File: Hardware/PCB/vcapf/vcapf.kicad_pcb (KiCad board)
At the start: 2 copper layers, 10 parts, among them J1 Synth_power_2x5

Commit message: Post breadboard tweaks; layout
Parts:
- removed the C2 at (238.3, 117.1)
- added C10: 100nF, ao_tht:C_Disc_D3.0mm_W1.6mm_P2.50mm, B.Cu at (111.4, 138.1)
- added C11: 100nF, ao_tht:C_Rect_L7.2mm_W2.5mm_P5.00mm_FKS2_FKP2_MKS2_MKP2, B.Cu at (84.8, 91.1)
- added C3: 100nF, ao_tht:C_Rect_L7.2mm_W2.5mm_P5.00mm_FKS2_FKP2_MKS2_MKP2, B.Cu at (115.2, 91.1)
- added C5: 100nF, ao_tht:C_Disc_D3.0mm_W1.6mm_P2.50mm, B.Cu at (111.5, 59.0)
- added C6: 4.7nF, ao_tht:C_Disc_D5.0mm_W2.5mm_P5.00mm, B.Cu at (86.0, 136.8)
- added C7: 100nF, ao_tht:C_Disc_D3.0mm_W1.6mm_P2.50mm, B.Cu at (91.1, 91.1)
- added C8: 100nF, ao_tht:C_Disc_D3.0mm_W1.6mm_P2.50mm, B.Cu at (111.4, 91.1)
- added C9: 100nF, ao_tht:C_Disc_D3.0mm_W1.6mm_P2.50mm, B.Cu at (96.2, 122.9)
- added D3: 1N4148, ao_tht:D_DO-35_SOD27_P7.62mm_Horizontal, B.Cu at (88.6, 74.6)
- added GRAF1: Holes, vcapf:vcapf_panel_holes, F.Cu at (100.0, 100.0)
- added GRAF2: CC0 logo, ao_tht:CC0_logo, F.Cu at (119.0, 169.1)
- added GRAF3: AO logo, ao_tht:analogoutput, B.Cu at (99.5, 75.0)
- added H1: MountingHole, ao_tht:MountingHole_3.2mm_M3, F.Cu at (80.0, 139.0)
- added H2: MountingHole, ao_tht:MountingHole_3.2mm_M3, F.Cu at (120.0, 139.0)
- added H3: MountingHole, ao_tht:MountingHole_3.2mm_M3, F.Cu at (180.0, 139.0)
- added H4: MountingHole, ao_tht:MountingHole_3.2mm_M3, F.Cu at (220.0, 139.0)
- added J2: AudioJack2, ao_tht:Jack_6.35mm_PJ_629HAN_slots, F.Cu at (187.5, 150.0)
- added J3: AudioJack2, ao_tht:Jack_6.35mm_PJ_629HAN_slots, F.Cu at (212.5, 150.0)
- added J4: Conn_01x05, Connector_PinSocket_2.54mm:PinSocket_1x05_P2.54mm_Vertical, B.Cu at (95.0, 138.5)
- added J5: Conn_01x05, Connector_PinHeader_2.54mm:PinHeader_1x05_P2.54mm_Vertical, F.Cu at (195.0, 138.5)
- added J6: AudioJack2, ao_tht:Jack_6.35mm_PJ_629HAN_slots, F.Cu at (187.5, 175.0)
- added J7: AudioJack2, ao_tht:Jack_6.35mm_PJ_629HAN_slots, F.Cu at (212.5, 175.0)
- added Q1: 2N3906, ao_tht:TO-92_Inline_Wide, B.Cu at (81.0, 120.0)
- added Q2: 2N3906, ao_tht:TO-92_Inline_Wide, B.Cu at (81.0, 112.3)
- added R1: 100k, ao_tht:R_Axial_DIN0207_L6.3mm_D2.5mm_P10.16mm_Horizontal, B.Cu at (119.0, 55.5)
- added R10: 4.7k, ao_tht:R_Axial_DIN0207_L6.3mm_D2.5mm_P10.16mm_Horizontal, B.Cu at (81.0, 126.7)
- added R11: 100k, ao_tht:R_Axial_DIN0207_L6.3mm_D2.5mm_P10.16mm_Horizontal, B.Cu at (81.0, 55.5)
- added R12: 620R, ao_tht:R_Axial_DIN0207_L6.3mm_D2.5mm_P10.16mm_Horizontal, B.Cu at (91.1, 51.7)
- added R13: 100k, ao_tht:R_Axial_DIN0207_L6.3mm_D2.5mm_P10.16mm_Horizontal, B.Cu at (81.0, 87.3)
- added R14: 620R, ao_tht:R_Axial_DIN0207_L6.3mm_D2.5mm_P10.16mm_Horizontal, B.Cu at (91.1, 47.9)
- added R15: 6.8k, ao_tht:R_Axial_DIN0207_L6.3mm_D2.5mm_P10.16mm_Horizontal, B.Cu at (81.0, 44.1)
- added R16: 30k, ao_tht:R_Axial_DIN0207_L6.3mm_D2.5mm_P10.16mm_Horizontal, B.Cu at (108.9, 98.7)
- added R17: 15k, ao_tht:R_Axial_DIN0207_L6.3mm_D2.5mm_P10.16mm_Horizontal, B.Cu at (108.9, 94.9)
- added R18: 30k, ao_tht:R_Axial_DIN0207_L6.3mm_D2.5mm_P10.16mm_Horizontal, B.Cu at (91.1, 102.5)
- added R19: 7.5k, ao_tht:R_Axial_DIN0207_L6.3mm_D2.5mm_P10.16mm_Horizontal, B.Cu at (91.1, 98.7)
- added R2: 470k, ao_tht:R_Axial_DIN0207_L6.3mm_D2.5mm_P10.16mm_Horizontal, B.Cu at (81.0, 70.8)
- added R20: 7.5k, ao_tht:R_Axial_DIN0207_L6.3mm_D2.5mm_P10.16mm_Horizontal, B.Cu at (91.1, 94.9)
- added R21: 10k, ao_tht:R_Axial_DIN0207_L6.3mm_D2.5mm_P10.16mm_Horizontal, B.Cu at (108.9, 126.7)
- added R22: 30k, ao_tht:R_Axial_DIN0207_L6.3mm_D2.5mm_P10.16mm_Horizontal, B.Cu at (119.0, 102.5)
- added R23: 30k, ao_tht:R_Axial_DIN0207_L6.3mm_D2.5mm_P10.16mm_Horizontal, B.Cu at (81.0, 106.3)
- added R24: 10k, ao_tht:R_Axial_DIN0207_L6.3mm_D2.5mm_P10.16mm_Horizontal, B.Cu at (119.0, 131.8)
- added R25: 100k, ao_tht:R_Axial_DIN0207_L6.3mm_D2.5mm_P10.16mm_Horizontal, B.Cu at (195.2, 163.5)
- added R26: 100k, ao_tht:R_Axial_DIN0207_L6.3mm_D2.5mm_P10.16mm_Horizontal, B.Cu at (209.2, 163.5)
- added R27: 1k, ao_tht:R_Axial_DIN0207_L6.3mm_D2.5mm_P10.16mm_Horizontal, B.Cu at (190.2, 163.5)
- added R28: 1k, ao_tht:R_Axial_DIN0207_L6.3mm_D2.5mm_P10.16mm_Horizontal, B.Cu at (200.3, 167.3)
- added R3: 100k, ao_tht:R_Axial_DIN0207_L6.3mm_D2.5mm_P10.16mm_Horizontal, B.Cu at (91.1, 78.4)
- added R4: 2.7k, ao_tht:R_Axial_DIN0207_L6.3mm_D2.5mm_P10.16mm_Horizontal, B.Cu at (81.0, 82.2)
- added R5: 620R, ao_tht:R_Axial_DIN0207_L6.3mm_D2.5mm_P10.16mm_Horizontal, B.Cu at (108.9, 51.7)
- added R6: 100k, ao_tht:R_Axial_DIN0207_L6.3mm_D2.5mm_P10.16mm_Horizontal, B.Cu at (119.0, 87.3)
- added R7: 620R, ao_tht:R_Axial_DIN0207_L6.3mm_D2.5mm_P10.16mm_Horizontal, B.Cu at (108.9, 47.9)
- added R8: 470k, ao_tht:R_Axial_DIN0207_L6.3mm_D2.5mm_P10.16mm_Horizontal, B.Cu at (81.0, 131.8)
- added R9: 6.8k, ao_tht:R_Axial_DIN0207_L6.3mm_D2.5mm_P10.16mm_Horizontal, B.Cu at (119.0, 44.1)
- added RV1: 100k, ao_tht:Potentiometer_Alpha_16mm_Single_Vertical, F.Cu at (100.0, 115.0)
- added RV2: 100k, ao_tht:Potentiometer_Alpha_16mm_Single_Vertical, F.Cu at (100.0, 30.0)
- added RV3: 100k, ao_tht:Potentiometer_Alpha_16mm_Single_Vertical, F.Cu at (99.7, 75.0)
- added U1: LM13700, ao_tht:DIP-16_W7.62mm_Socket_LongPads, B.Cu at (103.8, 44.1)
- added U2: TL074, ao_tht:DIP-14_W7.62mm_Socket_LongPads, B.Cu at (96.2, 102.5)
- added U3: TL072, ao_tht:DIP-8_W7.62mm_Socket_LongPads, B.Cu at (103.8, 126.7)
- C1, C4, D1, D2, J1: moved to B.Cu
- C2: renamed from C3; moved to B.Cu
- TP1: value TestPoint -> +12V; moved to B.Cu
- TP2: value TestPoint -> GND; footprint ao_tht:TestPoint_THTPad_D1.5mm_Drill0.7mm -> ao_tht:TestPoint_THTPad_1.5x1.5mm_Drill0.7mm; moved to B.Cu
- TP3: value TestPoint -> -12V; moved to B.Cu
- moved TP3 202.7 mm to (78.4, 25.1), turned to 90 degrees
- moved TP2 202.6 mm to (78.4, 32.7), turned to 90 degrees
- moved TP1 193.0 mm to (78.4, 40.3), turned to 90 degrees
- moved C1 189.1 mm to (82.2, 18.7)
- moved D2 177.0 mm to (91.1, 20.0)
- moved D1 176.8 mm to (91.1, 16.2)
- moved C2 176.2 mm to (106.3, 18.7)
- moved C4 163.5 mm to (91.0, 59.4), turned to 180 degrees
- moved J1 141.5 mm to (115.2, 34.0)
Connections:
- C4 pad 1: GND -> +12V
- C4 pad 2: -12V -> GND
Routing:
- net -12V: track 0.00 -> 190.1 mm
- net +12V: track 0.00 -> 157.5 mm
- net Net-(Q2-Pad3): track 0.00 -> 109.4 mm
- net /Main PCB/INPUT_ATT: track 0.00 -> 88.3 mm
- net /Main PCB/CV_IN: track 0.00 -> 88.0 mm
- net /Main PCB/LP1: track 0.00 -> 80.3 mm
- net Net-(D3-Pad1): track 0.00 -> 58.7 mm
- net Net-(R11-Pad2): track 0.00 -> 54.4 mm
- net Net-(C11-Pad1): track 0.00 -> 53.6 mm
- net Net-(C3-Pad1): track 0.00 -> 53.6 mm
- net /Main PCB/1POLE_OUT: track 0.00 -> 52.7 mm
- net /Main PCB/INPUT: track 0.00 -> 48.3 mm
- net Net-(R1-Pad2): track 0.00 -> 45.5 mm
- net /Main PCB/FREQ: track 0.00 -> 43.2 mm
- net /2POLE_OUT_J: track 0.00 -> 39.3 mm
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- added copper zone on B.Cu, net GND
- added copper zone on F.Cu, net GND
- added copper zone on B.Cu, net GND1
- added copper zone on F.Cu, net GND1
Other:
- board outline added: 146 x 171 mm
- board text added: "Jacks board"
- board text added: "Rich Holmes / April 2022 CC0 1.0 Main board"
- board text added: "VCAPF"
- board text added: "VOLTAGE CONTROLLED ALL PASS FILTER"
- board text added: "https://github.com/holmesrichards/vcapf"

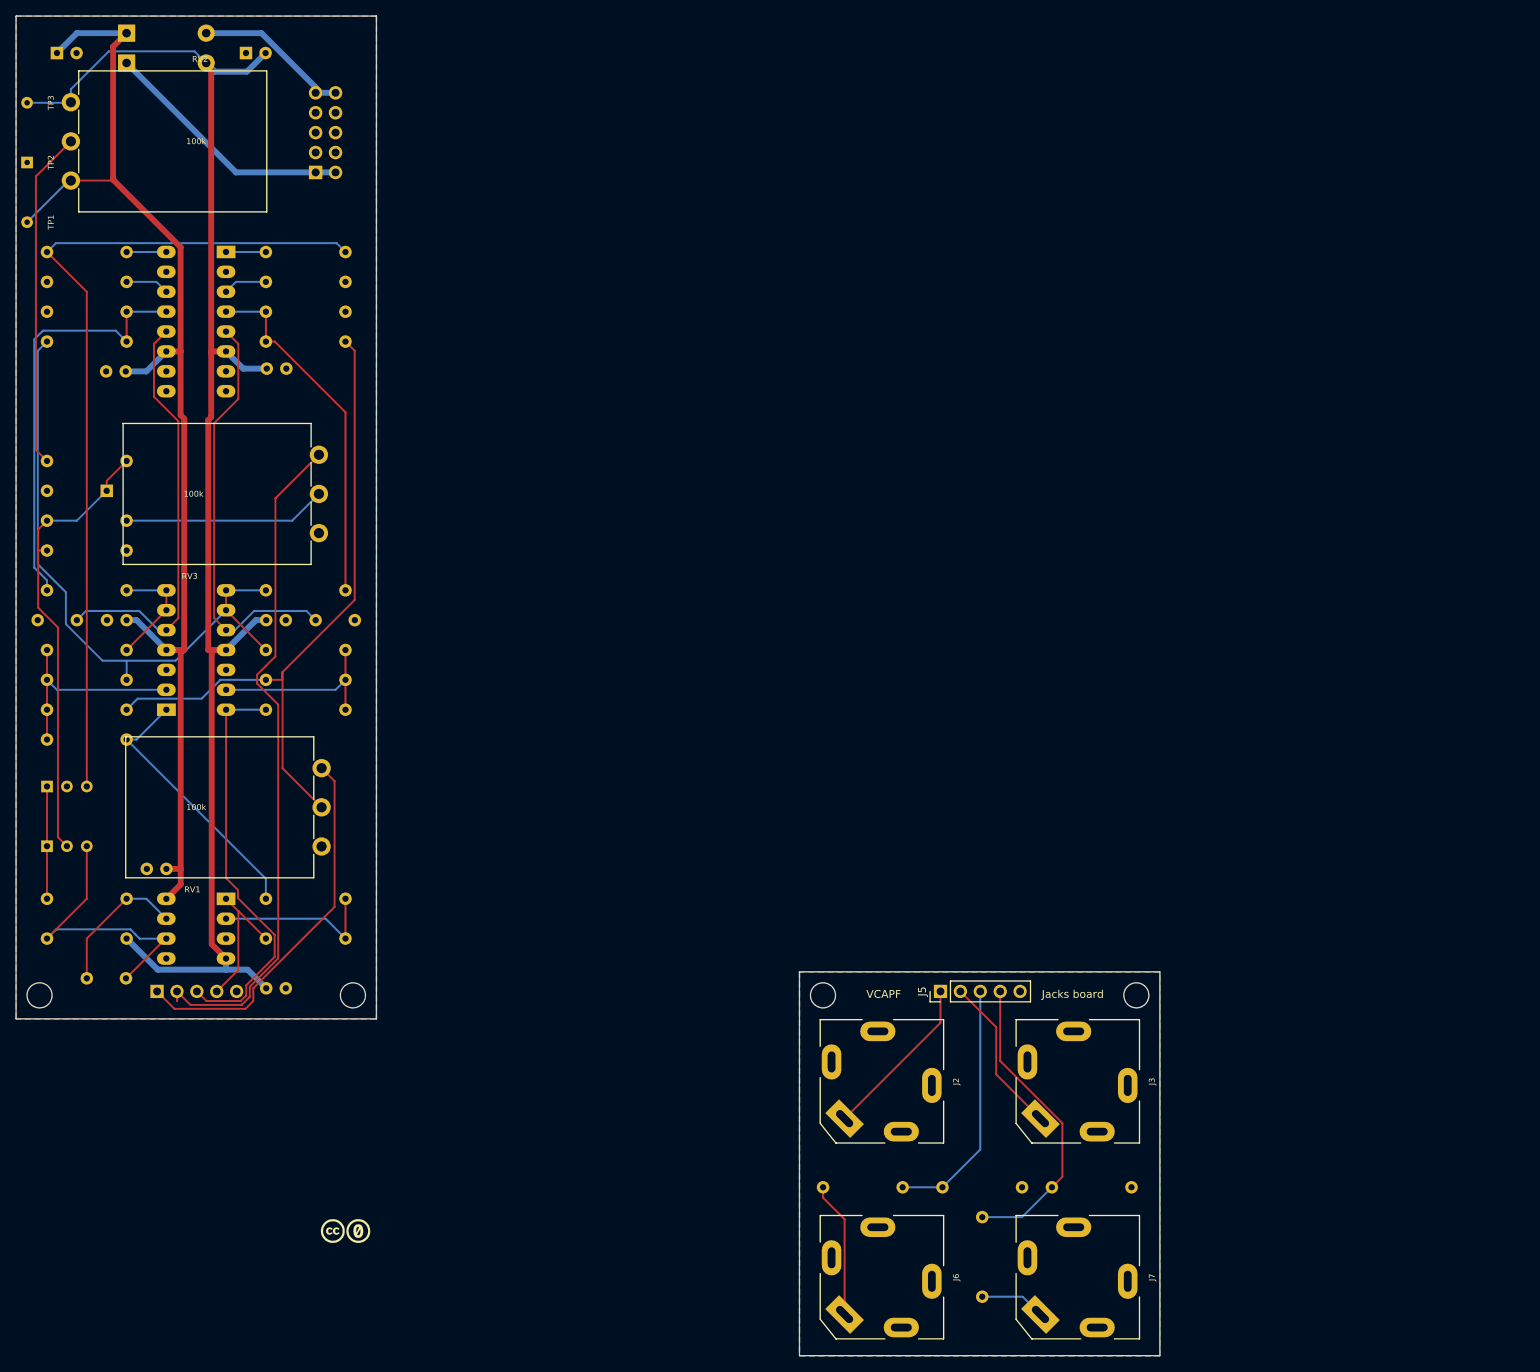
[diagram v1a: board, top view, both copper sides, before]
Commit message: Layout corrections, pot position and main board length
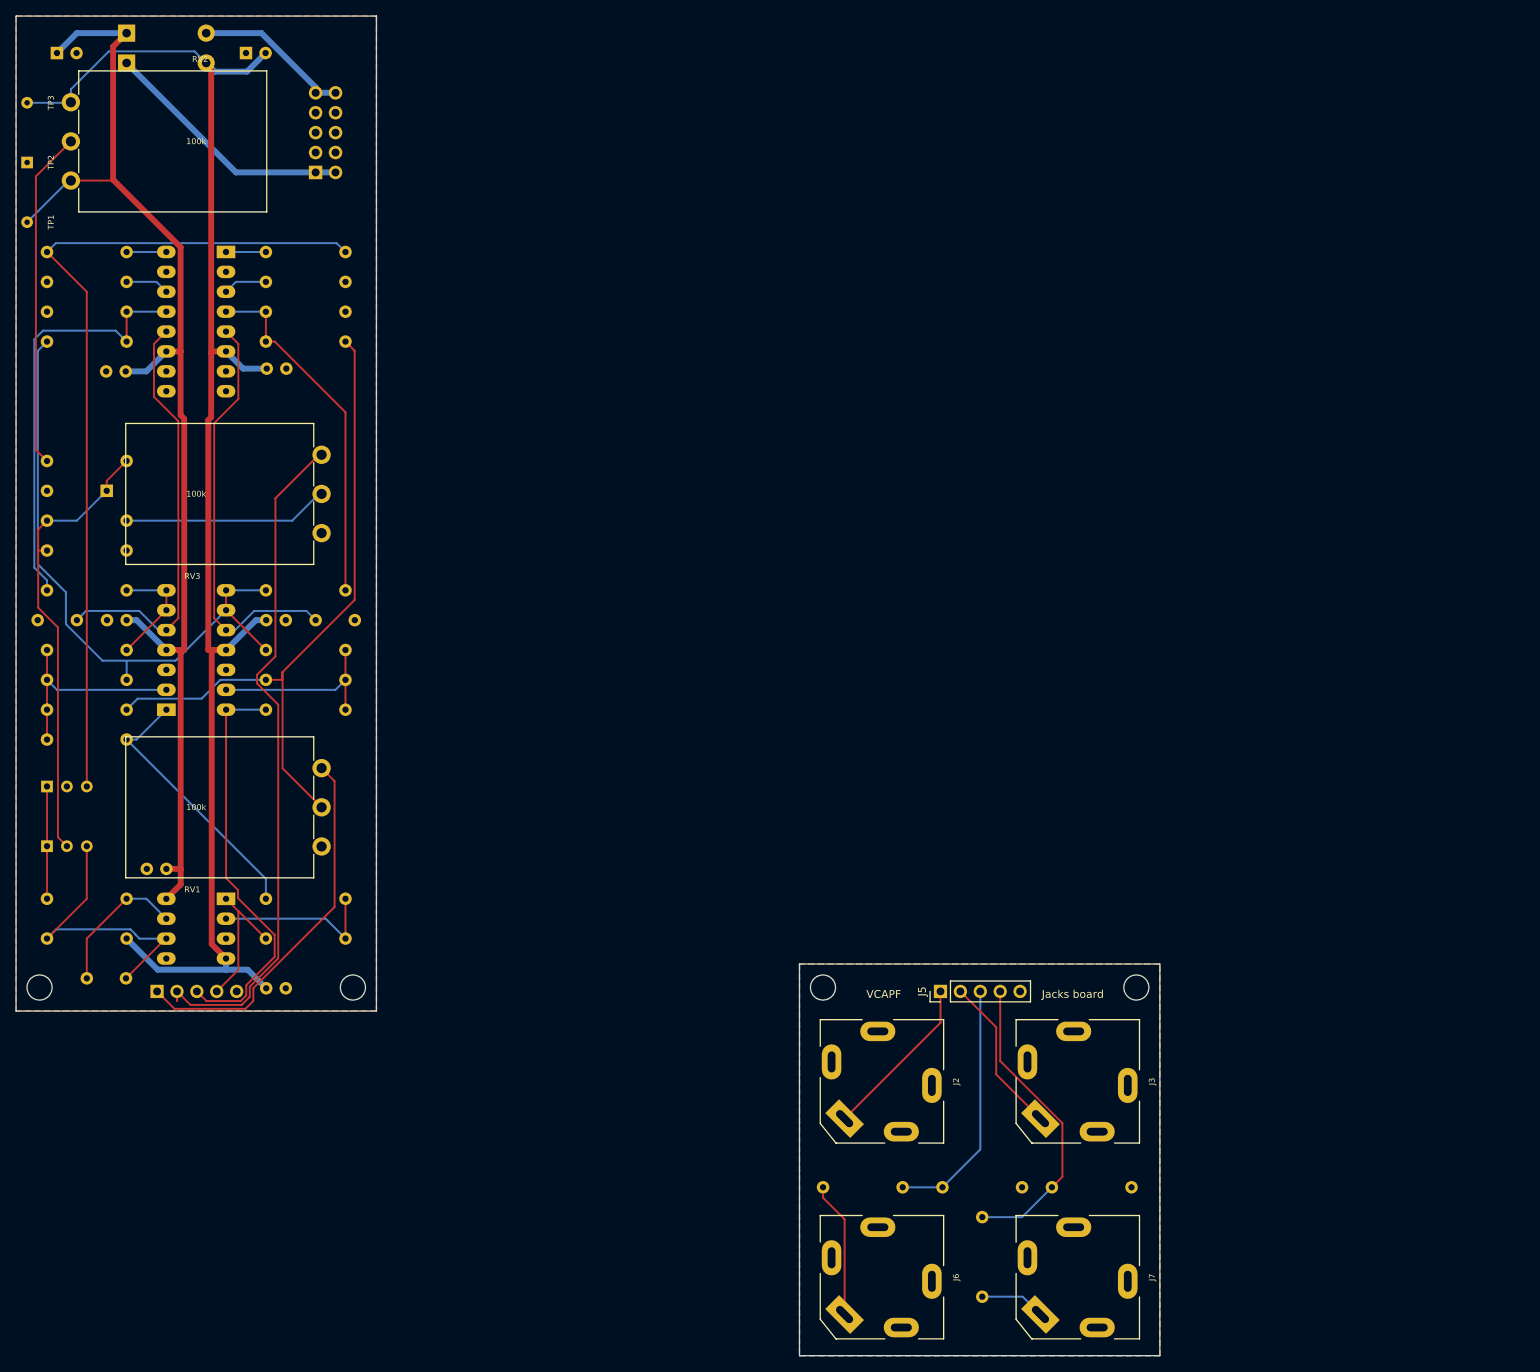
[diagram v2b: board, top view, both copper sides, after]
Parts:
- GRAF2: moved to B.Cu
- moved GRAF2 138.9 mm to (91.0, 33.0), turned to 180 degrees
- moved H1 1.00 mm to (80.0, 138.0)
- moved H2 1.00 mm to (120.0, 138.0)
- moved H3 1.00 mm to (180.0, 138.0)
- moved H4 1.00 mm to (220.0, 138.0)
- moved GRAF3 0.50 mm to (100.0, 75.0)
- moved RV3 0.34 mm to (100.0, 75.0)
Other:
- outline, holes or cut-outs redrawn

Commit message: Net labels, panel
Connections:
- net Net-(J6-PadS) renamed /1P OUT
- net Net-(J7-PadS) renamed /2P OUT
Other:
- board text added: "1P OUT"
- board text added: "2P OUT"
- board text added: "CV IN"
- board text added: "LFO IN"
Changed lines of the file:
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@@
   (net 41 "Net-(R21-Pad1)")
   (net 42 "Net-(C11-Pad1)")
-  (net 43 "Net-(J6-PadS)")
-  (net 44 "Net-(J7-PadS)")
+  (net 43 "/1P OUT")
+  (net 44 "/2P OUT")
   (footprint "ao_tht:Jack_6.35mm_PJ_629HAN_slots" (layer "F.Cu")
     (at 187.5 175 -90)
@@
     (pad "RN" thru_hole oval (at 6.4 -2.5 270) (size 2.500001 4.500001) (drill oval 1 2.7) (layers *.Cu *.Mask))
     (pad "S" thru_hole rect (at 4.74 4.74 315) (size 4.500001 2.500001) (drill oval 2.7 1) (layers *.Cu *.Mask)
-      (net 43 "Net-(J6-PadS)") (pintype "passive"))
+      (net 43 "/1P OUT") (pintype "passive"))
     (pad "T" thru_hole oval (at -6.4 0.5 270) (size 2.5 4.5) (drill oval 1 2.7) (layers *.Cu *.Mask)
       (net 22 "GND1") (pintype "passive"))
@@
     (pad "RN" thru_hole oval (at 6.4 -2.5 270) (size 2.500001 4.500001) (drill oval 1 2.7) (layers *.Cu *.Mask))
     (pad "S" thru_hole rect (at 4.74 4.74 315) (size 4.500001 2.500001) (drill oval 2.7 1) (layers *.Cu *.Mask)
-      (net 44 "Net-(J7-PadS)") (pintype "passive"))
+      (net 44 "/2P OUT") (pintype "passive"))
     (pad "T" thru_hole oval (at -6.4 0.5 270) (size 2.5 4.5) (drill oval 1 2.7) (layers *.Cu *.Mask)
       (net 22 "GND1") (pintype "passive"))
@@
       (net 28 "/1POLE_OUT_J") (pintype "passive"))
     (pad "2" thru_hole oval locked (at 10.16 0 180) (size 1.6 1.6) (drill 0.8) (layers *.Cu *.Mask)
-      (net 43 "Net-(J6-PadS)") (pintype "passive"))
+      (net 43 "/1P OUT") (pintype "passive"))
     (model "${KICAD_AOKICAD}/ao_tht_3d/R_Axial_DIN0207_L6.3mm_D2.5mm_P10.16mm_Horizontal.wrl"
       (offset (xyz 0 0 0))
@@
       (net 29 "/2POLE_OUT_J") (pintype "passive"))
     (pad "2" thru_hole oval locked (at 10.16 0 270) (size 1.6 1.6) (drill 0.8) (layers *.Cu *.Mask)
-      (net 44 "Net-(J7-PadS)") (pintype "passive"))
+      (net 44 "/2P OUT") (pintype "passive"))
     (model "${KICAD_AOKICAD}/ao_tht_3d/R_Axial_DIN0207_L6.3mm_D2.5mm_P10.16mm_Horizontal.wrl"
       (offset (xyz 0 0 0))
@@
     (effects (font (size 1 1) (thickness 0.15)) (justify mirror))
   )
+  (gr_text "1P OUT" (at 187.5 175) (layer "B.SilkS")
+    (effects (font (size 1 1) (thickness 0.15)) (justify mirror))
+  )
+  (gr_text "LFO IN" (at 187.5 150) (layer "B.SilkS")
+    (effects (font (size 1 1) (thickness 0.15)) (justify mirror))
+  )
+  (gr_text "CV IN" (at 212.5 150) (layer "B.SilkS")
+    (effects (font (size 1 1) (thickness 0.15)) (justify mirror))
+  )
   (gr_text "Rich Holmes / April 2022\nCC0 1.0\n\nMain board" (at 98.5 32.5) (layer "B.SilkS")
     (effects (font (size 1 1) (thickness 0.15)) (justify mirror))
   )
+  (gr_text "2P OUT" (at 212.5 175) (layer "B.SilkS")
+    (effects (font (size 1 1) (thickness 0.15)) (justify mirror))
+  )
